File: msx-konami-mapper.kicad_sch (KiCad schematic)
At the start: 12 parts, among them SW1 Bonus Games, U1 SST39SF040, U3 74LS670, U4 74LS02

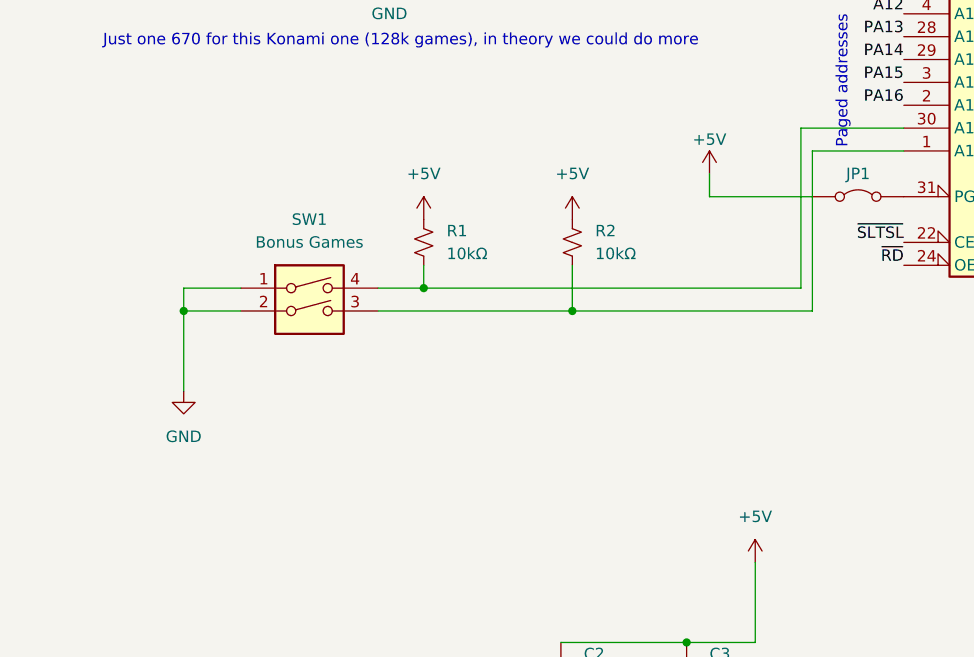
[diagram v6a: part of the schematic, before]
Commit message: Fix DIP switch being backward
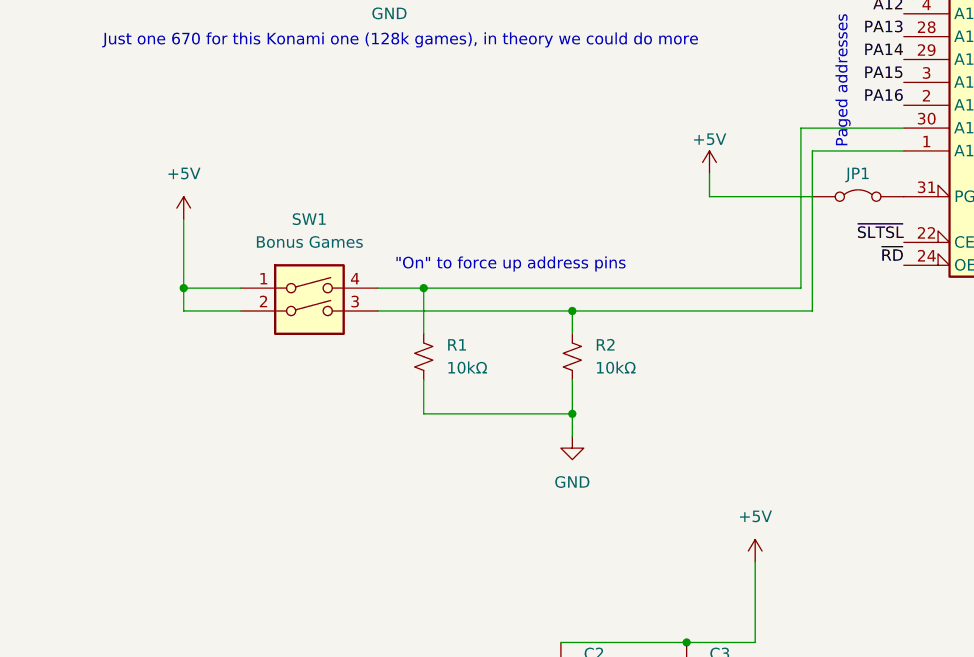
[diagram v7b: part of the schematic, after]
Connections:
- net +5V: now also SW1.1, SW1.2; no longer R1.1, R2.1
- net GND: now also R1.1, R2.1; no longer SW1.1, SW1.2
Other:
- note added: ""On" to force up address pins"
- moved on the sheet: R1, R2

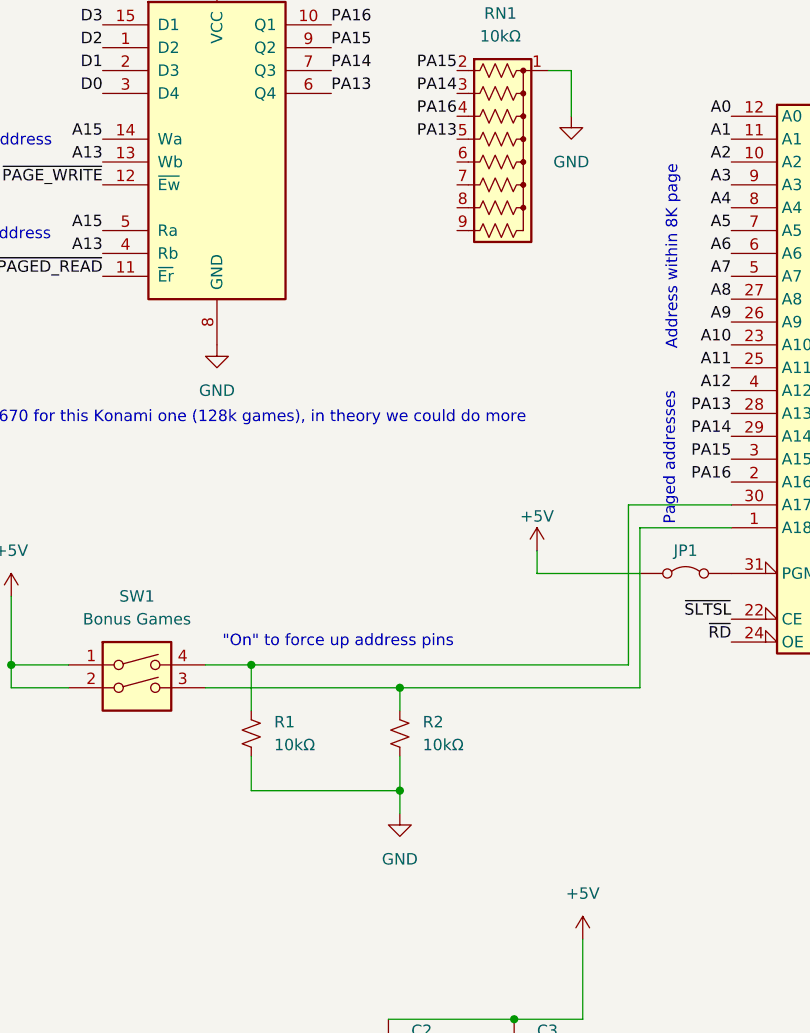
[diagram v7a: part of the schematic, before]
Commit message: Remove some parts
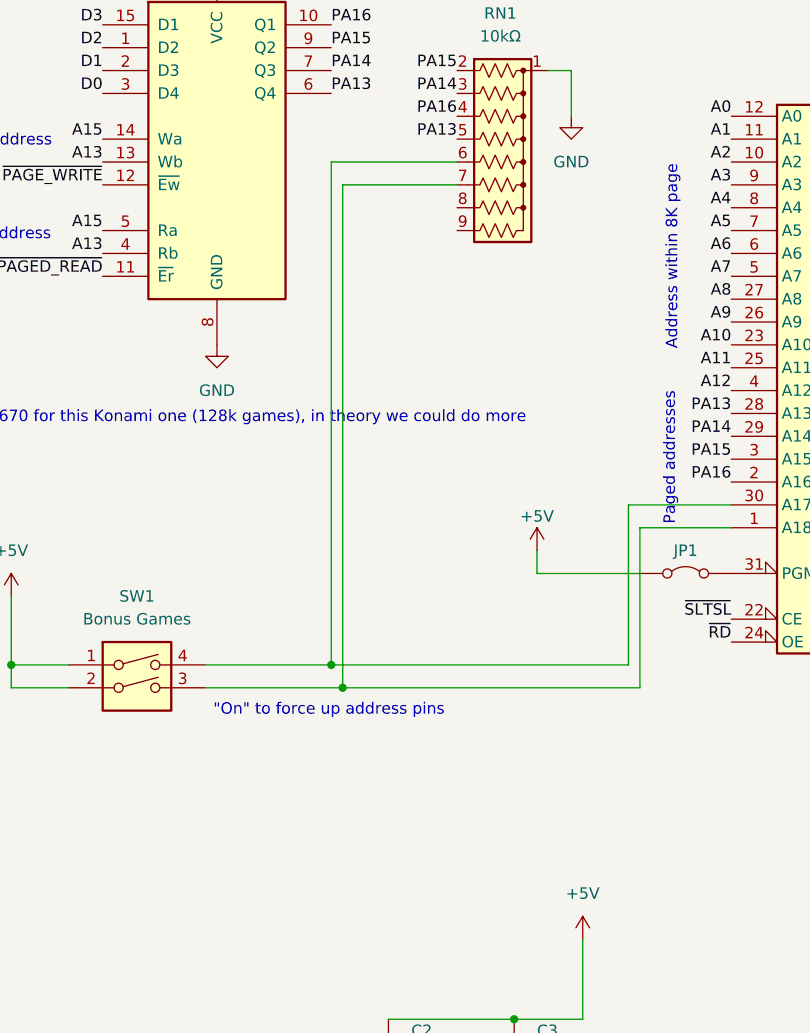
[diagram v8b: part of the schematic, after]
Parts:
- removed R1, R2: 10kΩ, Resistor_THT:R_Axial_DIN0207_L6.3mm_D2.5mm_P10.16mm_Horizontal, symbol Device:R_Small_US
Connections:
- net at SW1.3, U1.1 (A18): now also RN1.7 (R6)
- net at SW1.4, U1.30 (A17): now also RN1.6 (R5)
